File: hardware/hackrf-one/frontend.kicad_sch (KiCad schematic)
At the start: 145 parts, among them J10 GND_CLIP, J2 RF-SHIELD-FRAME, J3 RF-SHIELD-COVER, J4 MOUNTING_HOLE, J5 MOUNTING_HOLE, J6 MOUNTING_HOLE, J7 MOUNTING_HOLE, J8 MOUNTING_HOLE, J9 MOUNTING_HOLE, P13 GPO1, P17 GPO6, P19 GPO3, P21 REF_IN, P27 MIXER_SDATA, P31 MIXER_SCLK, P32 MIXER_ENX, P33 MIXER_RESETX, P34 MIX_BYPASS, P35 !MIX_BYPASS, P4 ANTENNA, P43 RX, P44 HP, P45 LP, P46 TX_MIX_BP, P47 RX_MIX_BP, P48 TX_AMP, P49 RX_AMP, P50 AMP_BYPASS, P51 !TX_AMP_PWR, P52 !RX_AMP_PWR, P6 GPO4, P7 GPO2, Q1 MOSFET_P, Q2 MOSFET_P, Q4 MOSFET_P, T1 MIX_IN_BALUN, T2 MIX_OUT_BALUN, U1 SKY13453, U10 SKY13453, U11 SKY13453, U12 SKY13317, U13 MGA-81563, U14 SKY13317, U2 SKY13453, U25 MGA-81563, U3 RX_LOWPASS_FILTER, U4 RFFC5072, U5 SKY13453, U6 SKY13453, U7 SKY13453, U8 RX_HIGHPASS_FILTER, U9 SKY13317

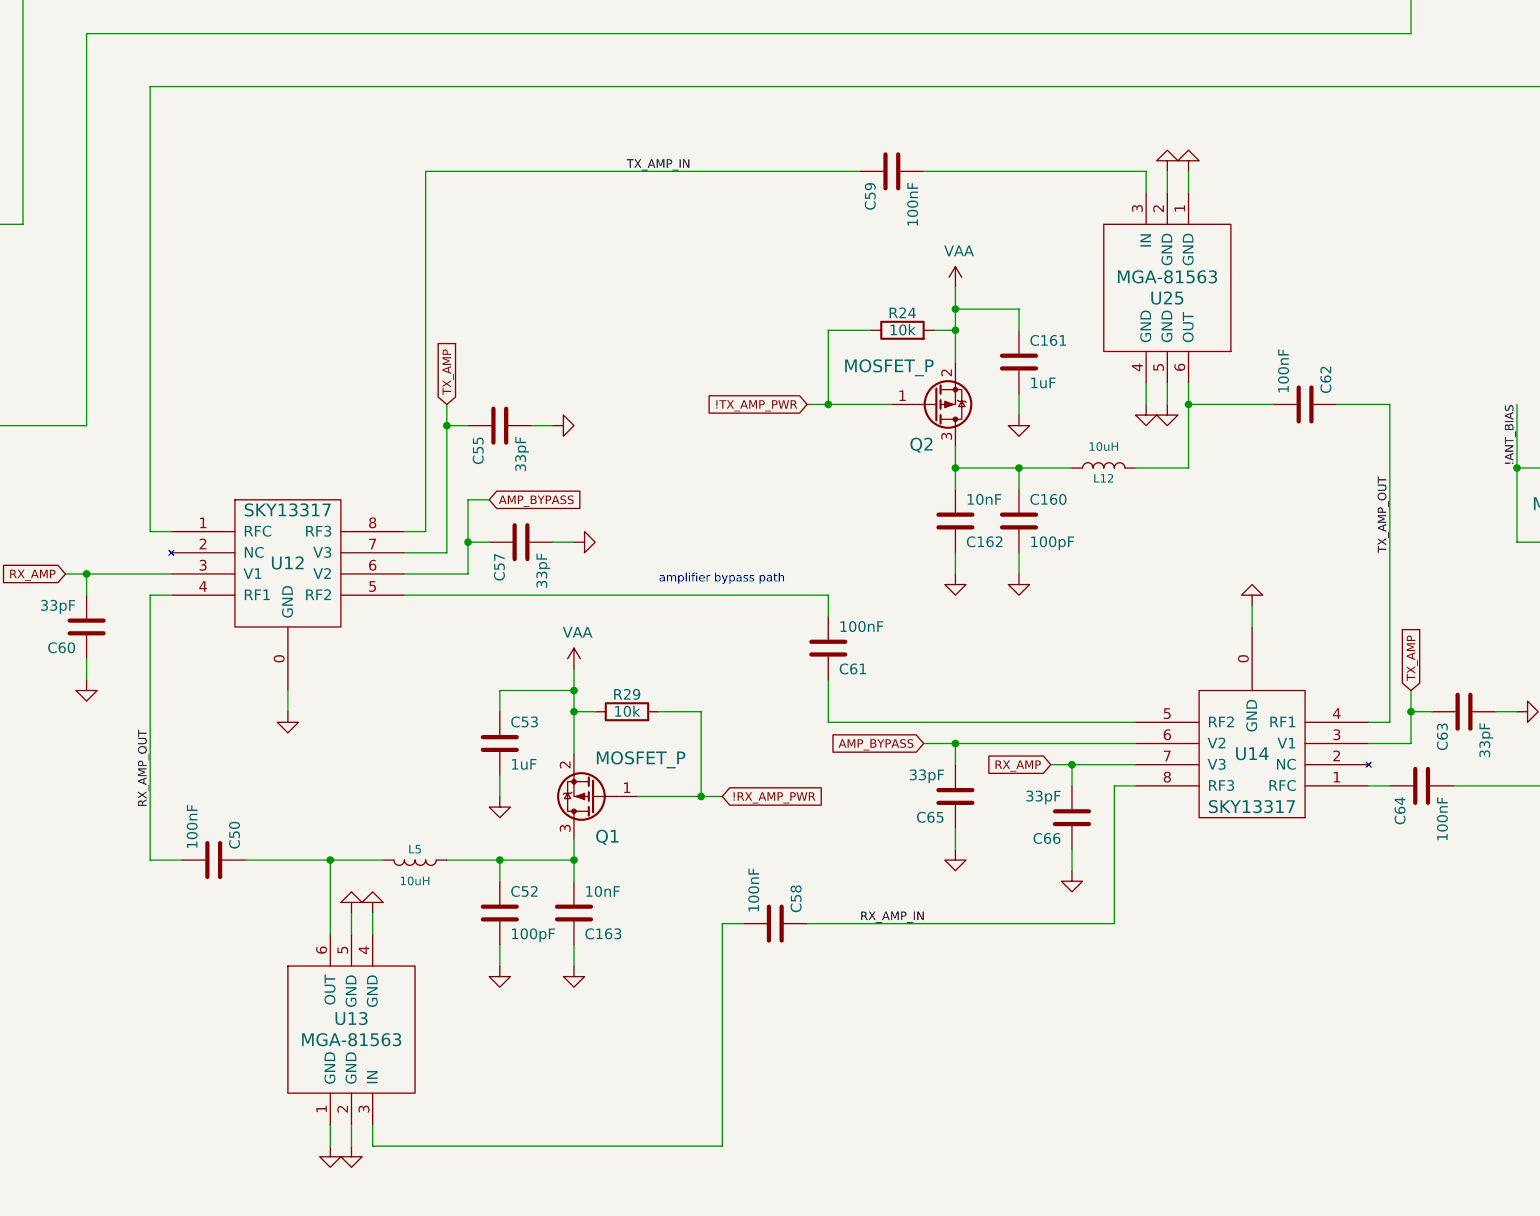
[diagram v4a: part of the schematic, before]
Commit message: HackRF One: add resistance to amplifier supplies
This may improve reliability since switching to a MOSFET with lower on
resistance.
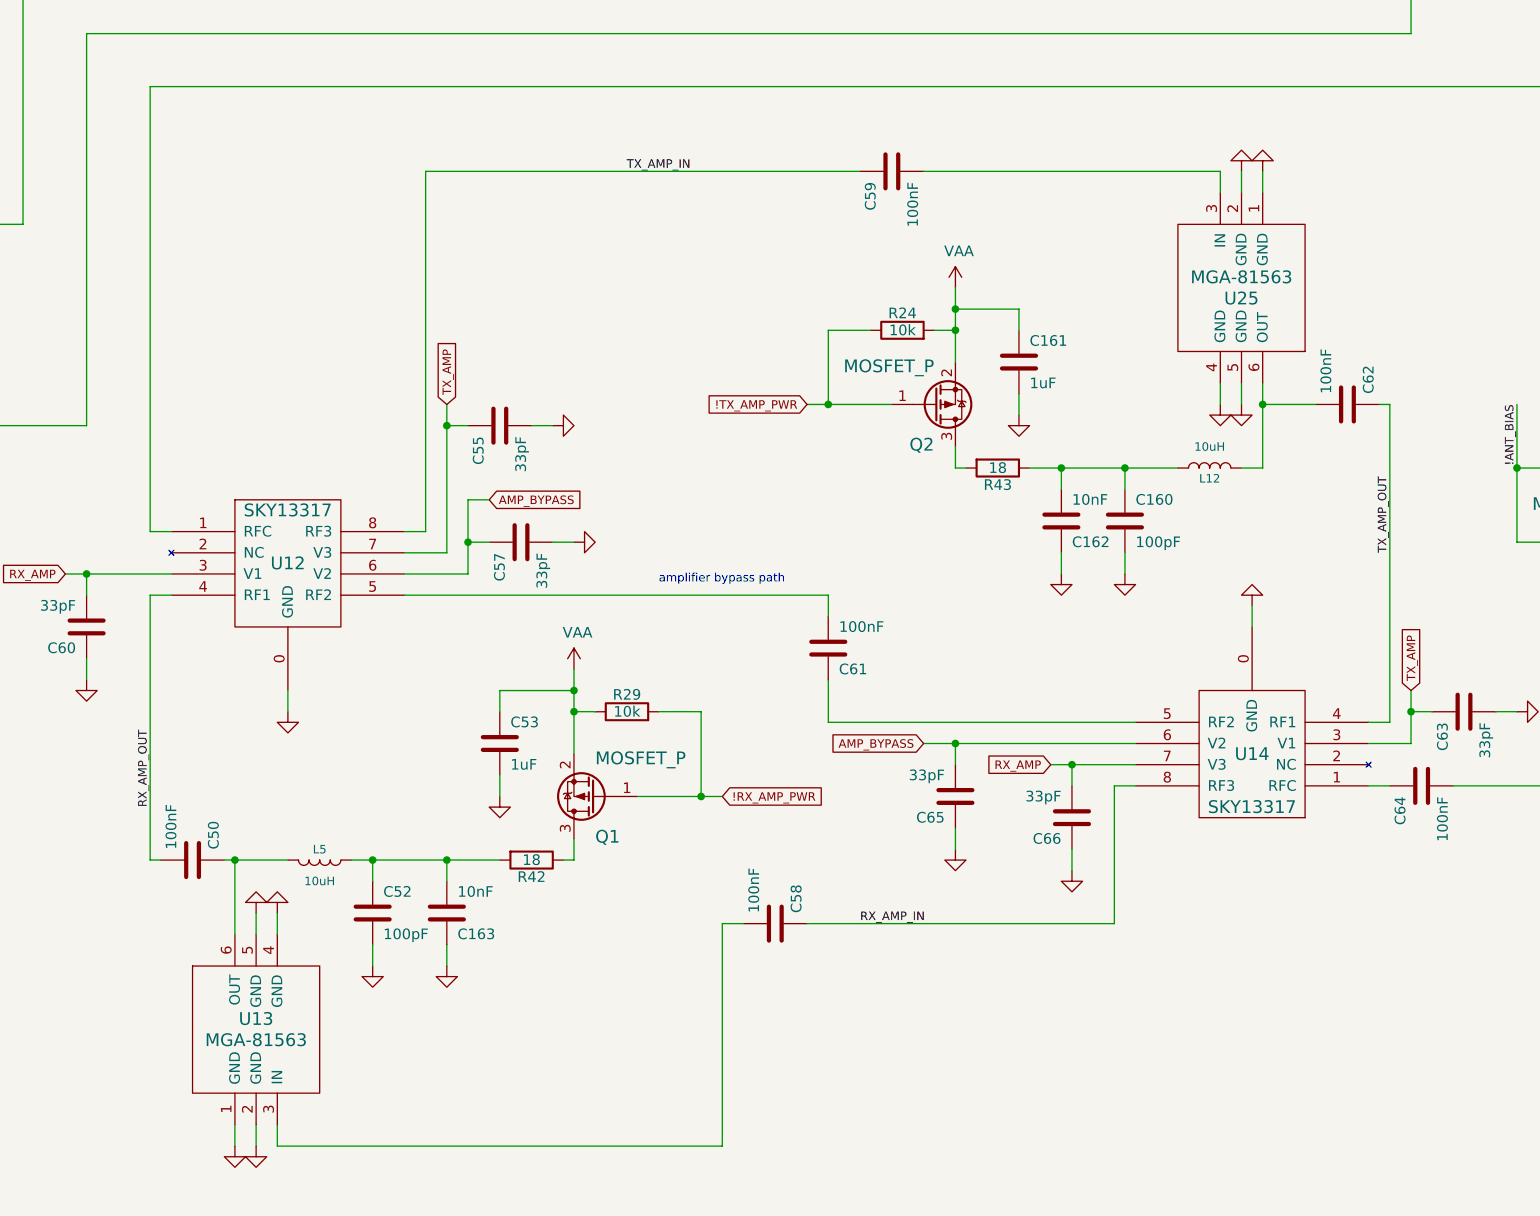
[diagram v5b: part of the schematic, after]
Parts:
- added R42, R43: 18, hackrf:GSG-0402, symbol Device:R
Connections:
- net at C163.2, C52.1, L5.1: now also R42.2; no longer Q1.3 (D)
- net at C160.1, C162.2, L12.1: now also R43.1; no longer Q2.3 (D)
- new net: Q1.3 (D), R42.1
- new net: Q2.3 (D), R43.2
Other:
- moved on the sheet: C160, C162, C163, C50, C52, C62, L12, L5, U13, U25

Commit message: HackRF One: update 100 nF capacitor part selection
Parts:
- C166, C17, C18, C20, C23, C25, C28, C31, C44, C46, C49, C50, C58, C59, C61, C62, C64, C9: Manufacturer Murata -> Samsung; Part Number GRM155R61A104KA01D -> CL05A104KA5NNNC; Substitution (none) -> Murata GRM155R61A104KA01D

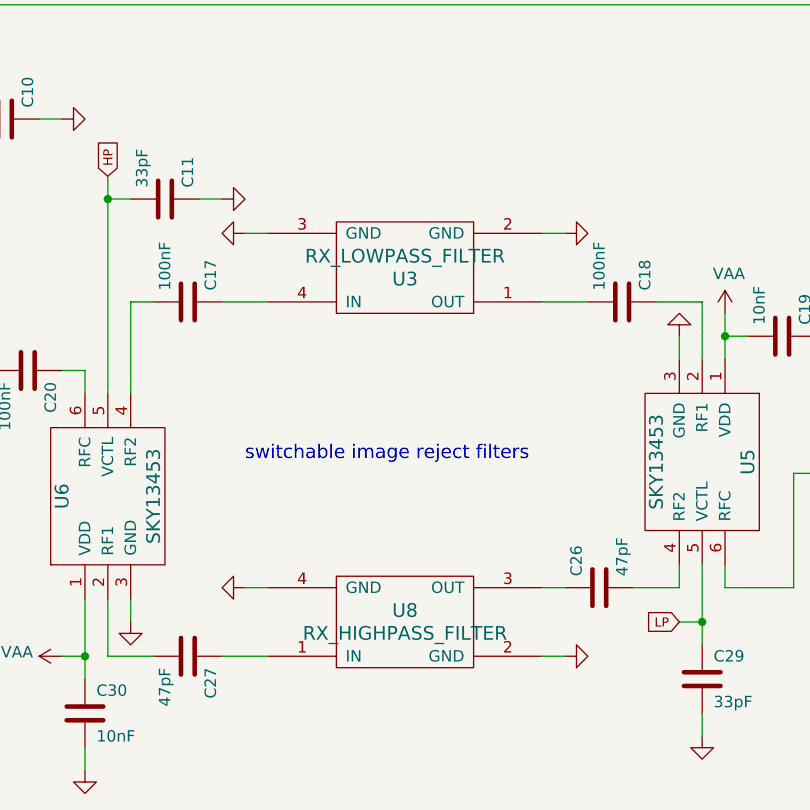
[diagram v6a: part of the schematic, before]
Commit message: HackRF One: clean up symbol value names
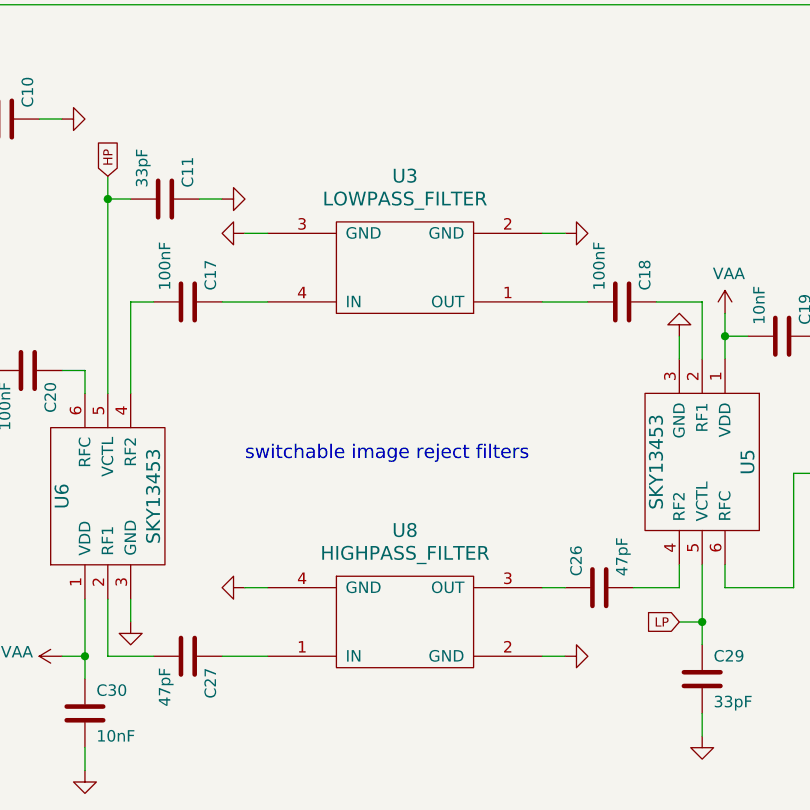
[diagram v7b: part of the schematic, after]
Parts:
- U3: value RX_LOWPASS_FILTER -> LOWPASS_FILTER
- U8: value RX_HIGHPASS_FILTER -> HIGHPASS_FILTER
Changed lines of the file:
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@@
   (symbol (lib_id "hackrf:FIL-DEA") (at 289.56 97.79 0) (unit 1)
     (in_bom yes) (on_board yes)
-    (property "Reference" "U8" (id 0) (at 289.56 96.52 0)
+    (property "Reference" "U8" (id 0) (at 289.56 87.63 0)
       (effects (font (size 1.524 1.524)))
     )
-    (property "Value" "RX_HIGHPASS_FILTER" (id 1) (at 289.56 99.06 0)
+    (property "Value" "HIGHPASS_FILTER" (id 1) (at 289.56 90.17 0)
       (effects (font (size 1.524 1.524)))
     )
@@
   (symbol (lib_id "hackrf:FIL-LP0603") (at 289.56 58.42 180) (unit 1)
     (in_bom yes) (on_board yes)
-    (property "Reference" "U3" (id 0) (at 289.56 59.69 0)
+    (property "Reference" "U3" (id 0) (at 289.56 48.26 0)
       (effects (font (size 1.524 1.524)))
     )
-    (property "Value" "RX_LOWPASS_FILTER" (id 1) (at 289.56 57.15 0)
+    (property "Value" "LOWPASS_FILTER" (id 1) (at 289.56 50.8 0)
       (effects (font (size 1.524 1.524)))
     )

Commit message: HackRF One: correct fabrication attributes and DNP
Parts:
- J3: footprint hackrf:GSG-NULL-MODULE -> (none)
- J4, J5, J6, J7, J8, J9, P13, P17, P19, P21, P27, P31, P32, P33, P34, P35, P43, P44, P45, P46, P47, P48, P49, P50, P51, P52, P6, P7: DNP DNP -> (none); now left out of the parts list
- JP1: now left out of the parts list
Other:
- moved on the sheet: C47, C7
